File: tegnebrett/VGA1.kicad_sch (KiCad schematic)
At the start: 47 parts, among them J4 DA15_Socket

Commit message: feat: add 100MHz oscillator footprint
Additionally add the footprint to PCB.
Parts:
- J4: footprint (none) -> tegnebrett_modules:AMPHENOL_L77HDE15SD1CH4RHNVGA
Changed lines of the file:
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@@
 			)
 		)
-		(property "Footprint" ""
+		(property "Footprint" "tegnebrett_modules:AMPHENOL_L77HDE15SD1CH4RHNVGA"
 			(at 255.27 118.11 0)
 			(effects

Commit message: feat: add VGA Transceiver footprint
Additionally add VGA Transceiver to PCB layout.
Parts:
- U6: value ~ -> VGA Transceiver; footprint (none) -> tegnebrett_modules:SOP65P640X120-20N
- U7: value ~ -> VGA Transciever; footprint (none) -> tegnebrett_modules:SOP65P640X120-20N
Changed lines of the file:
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@@
 			)
 		)
-		(property "Value" "~"
+		(property "Value" "VGA Transciever"
 			(at 85.9633 128.27 0)
 			(effects
@@
 			)
 		)
-		(property "Footprint" ""
+		(property "Footprint" "tegnebrett_modules:SOP65P640X120-20N"
 			(at 78.74 128.27 0)
 			(effects
@@
 			)
 		)
-		(property "Value" "~"
+		(property "Value" "VGA Transceiver"
 			(at 80.8833 38.1 0)
 			(effects
@@
 			)
 		)
-		(property "Footprint" ""
+		(property "Footprint" "tegnebrett_modules:SOP65P640X120-20N"
 			(at 73.66 38.1 0)
 			(effects

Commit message: feat: add footprint for each capacitor
It's all 0805, 1206 or 1210 hand soldering variants.
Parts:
- C87, C88, C89, C90: footprint (none) -> Capacitor_SMD:C_0805_2012Metric_Pad1.18x1.45mm_HandSolder
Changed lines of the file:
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@@
 			)
 		)
-		(property "Footprint" ""
+		(property "Footprint" "Capacitor_SMD:C_0805_2012Metric_Pad1.18x1.45mm_HandSolder"
 			(at 86.0552 119.38 0)
 			(effects
@@
 			)
 		)
-		(property "Footprint" ""
+		(property "Footprint" "Capacitor_SMD:C_0805_2012Metric_Pad1.18x1.45mm_HandSolder"
 			(at 80.9752 29.21 0)
 			(effects
@@
 			)
 		)
-		(property "Footprint" ""
+		(property "Footprint" "Capacitor_SMD:C_0805_2012Metric_Pad1.18x1.45mm_HandSolder"
 			(at 69.5452 29.21 0)
 			(effects
@@
 			)
 		)
-		(property "Footprint" ""
+		(property "Footprint" "Capacitor_SMD:C_0805_2012Metric_Pad1.18x1.45mm_HandSolder"
 			(at 74.6252 119.38 0)
 			(effects

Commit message: feat: add footprint to resistors
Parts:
- R23, R24, R25, R26, R27, R28, R29, R30, R31, R32, R33, R34, R35, R36, R37, R38, R39, R40, R41, R42, R43, R44, R45, R46, R47, R48, R49, R50, R51, R52, R53, R54, R55, R56, R57, R58, R59, R60, R61, R62: footprint (none) -> Resistor_SMD:R_0805_2012Metric_Pad1.20x1.40mm_HandSolder
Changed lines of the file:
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@@
 			)
 		)
-		(property "Footprint" ""
+		(property "Footprint" "Resistor_SMD:R_0805_2012Metric_Pad1.20x1.40mm_HandSolder"
 			(at 35.052 171.45 90)
 			(effects
@@
 			)
 		)
-		(property "Footprint" ""
+		(property "Footprint" "Resistor_SMD:R_0805_2012Metric_Pad1.20x1.40mm_HandSolder"
 			(at 38.862 81.28 90)
 			(effects
@@
 			)
 		)
-		(property "Footprint" ""
+		(property "Footprint" "Resistor_SMD:R_0805_2012Metric_Pad1.20x1.40mm_HandSolder"
 			(at 125.222 54.61 90)
 			(effects
@@
 			)
 		)
-		(property "Footprint" ""
+		(property "Footprint" "Resistor_SMD:R_0805_2012Metric_Pad1.20x1.40mm_HandSolder"
 			(at 125.222 31.75 90)
 			(effects
@@
 			)
 		)
-		(property "Footprint" ""
+		(property "Footprint" "Resistor_SMD:R_0805_2012Metric_Pad1.20x1.40mm_HandSolder"
 			(at 166.37 62.738 90)
 			(effects
@@
 			)
 		)
-		(property "Footprint" ""
+		(property "Footprint" "Resistor_SMD:R_0805_2012Metric_Pad1.20x1.40mm_HandSolder"
 			(at 115.57 103.378 90)
 			(effects
@@
 			)
 		)
-		(property "Footprint" ""
+		(property "Footprint" "Resistor_SMD:R_0805_2012Metric_Pad1.20x1.40mm_HandSolder"
 			(at 49.022 35.56 90)
 			(effects
@@
 			)
 		)
-		(property "Footprint" ""
+		(property "Footprint" "Resistor_SMD:R_0805_2012Metric_Pad1.20x1.40mm_HandSolder"
 			(at 115.57 39.878 90)
 			(effects
@@
 			)
 		)
-		(property "Footprint" ""
+		(property "Footprint" "Resistor_SMD:R_0805_2012Metric_Pad1.20x1.40mm_HandSolder"
 			(at 31.242 35.56 90)
 			(effects
@@
 			)
 		)
-		(property "Footprint" ""
+		(property "Footprint" "Resistor_SMD:R_0805_2012Metric_Pad1.20x1.40mm_HandSolder"
 			(at 40.132 35.56 90)
 			(effects
@@
 			)
 		)
-		(property "Footprint" ""
+		(property "Footprint" "Resistor_SMD:R_0805_2012Metric_Pad1.20x1.40mm_HandSolder"
 			(at 125.222 118.11 90)
 			(effects
@@
 			)
 		)
-		(property "Footprint" ""
+		(property "Footprint" "Resistor_SMD:R_0805_2012Metric_Pad1.20x1.40mm_HandSolder"
 			(at 115.57 51.308 90)
 			(effects
@@
 			)
 		)
-		(property "Footprint" ""
+		(property "Footprint" "Resistor_SMD:R_0805_2012Metric_Pad1.20x1.40mm_HandSolder"
 			(at 237.49 124.968 90)
 			(effects
@@
 			)
 		)
-		(property "Footprint" ""
+		(property "Footprint" "Resistor_SMD:R_0805_2012Metric_Pad1.20x1.40mm_HandSolder"
 			(at 43.942 171.45 90)
 			(effects
@@
 			)
 		)
-		(property "Footprint" ""
+		(property "Footprint" "Resistor_SMD:R_0805_2012Metric_Pad1.20x1.40mm_HandSolder"
 			(at 125.222 129.54 90)
 			(effects
@@
 			)
 		)
-		(property "Footprint" ""
+		(property "Footprint" "Resistor_SMD:R_0805_2012Metric_Pad1.20x1.40mm_HandSolder"
 			(at 176.022 54.61 90)
 			(effects
@@
 			)
 		)
-		(property "Footprint" ""
+		(property "Footprint" "Resistor_SMD:R_0805_2012Metric_Pad1.20x1.40mm_HandSolder"
 			(at 115.57 62.738 90)
 			(effects
@@
 			)
 		)
-		(property "Footprint" ""
+		(property "Footprint" "Resistor_SMD:R_0805_2012Metric_Pad1.20x1.40mm_HandSolder"
 			(at 54.102 125.73 90)
 			(effects
@@
 			)
 		)
-		(property "Footprint" ""
+		(property "Footprint" "Resistor_SMD:R_0805_2012Metric_Pad1.20x1.40mm_HandSolder"
 			(at 115.57 114.808 90)
 			(effects
@@
 			)
 		)
-		(property "Footprint" ""
+		(property "Footprint" "Resistor_SMD:R_0805_2012Metric_Pad1.20x1.40mm_HandSolder"
 			(at 176.022 43.18 90)
 			(effects
@@
 			)
 		)
-		(property "Footprint" ""
+		(property "Footprint" "Resistor_SMD:R_0805_2012Metric_Pad1.20x1.40mm_HandSolder"
 			(at 125.222 106.68 90)
 			(effects
@@
 			)
 		)
-		(property "Footprint" ""
+		(property "Footprint" "Resistor_SMD:R_0805_2012Metric_Pad1.20x1.40mm_HandSolder"
 			(at 166.37 74.168 90)
 			(effects
@@
 			)
 		)
-		(property "Footprint" ""
+		(property "Footprint" "Resistor_SMD:R_0805_2012Metric_Pad1.20x1.40mm_HandSolder"
 			(at 166.37 41.148 90)
 			(effects
@@
 			)
 		)
-		(property "Footprint" ""
+		(property "Footprint" "Resistor_SMD:R_0805_2012Metric_Pad1.20x1.40mm_HandSolder"
 			(at 125.222 66.04 90)
 			(effects
@@
 			)
 		)
-		(property "Footprint" ""
+		(property "Footprint" "Resistor_SMD:R_0805_2012Metric_Pad1.20x1.40mm_HandSolder"
 			(at 47.752 81.28 90)
 			(effects
@@
 			)
 		)
-		(property "Footprint" ""
+		(property "Footprint" "Resistor_SMD:R_0805_2012Metric_Pad1.20x1.40mm_HandSolder"
 			(at 45.212 125.73 90)
 			(effects
@@
 			)
 		)
-		(property "Footprint" ""
+		(property "Footprint" "Resistor_SMD:R_0805_2012Metric_Pad1.20x1.40mm_HandSolder"
 			(at 29.972 81.28 90)
 			(effects
@@
 			)
 		)
-		(property "Footprint" ""
+		(property "Footprint" "Resistor_SMD:R_0805_2012Metric_Pad1.20x1.40mm_HandSolder"
 			(at 57.912 35.56 90)
 			(effects
@@
 			)
 		)
-		(property "Footprint" ""
+		(property "Footprint" "Resistor_SMD:R_0805_2012Metric_Pad1.20x1.40mm_HandSolder"
 			(at 166.37 51.308 90)
 			(effects
@@
 			)
 		)
-		(property "Footprint" ""
+		(property "Footprint" "Resistor_SMD:R_0805_2012Metric_Pad1.20x1.40mm_HandSolder"
 			(at 176.022 77.47 90)
 			(effects
@@
 			)
 		)
-		(property "Footprint" ""
+		(property "Footprint" "Resistor_SMD:R_0805_2012Metric_Pad1.20x1.40mm_HandSolder"
 			(at 115.57 93.218 90)
 			(effects
@@
 			)
 		)
-		(property "Footprint" ""
+		(property "Footprint" "Resistor_SMD:R_0805_2012Metric_Pad1.20x1.40mm_HandSolder"
 			(at 56.642 81.28 90)
 			(effects
@@
 			)
 		)
-		(property "Footprint" ""
+		(property "Footprint" "Resistor_SMD:R_0805_2012Metric_Pad1.20x1.40mm_HandSolder"
 			(at 115.57 126.238 90)
 			(effects
@@
 			)
 		)
-		(property "Footprint" ""
+		(property "Footprint" "Resistor_SMD:R_0805_2012Metric_Pad1.20x1.40mm_HandSolder"
 			(at 176.022 66.04 90)
 			(effects
@@
 			)
 		)
-		(property "Footprint" ""
+		(property "Footprint" "Resistor_SMD:R_0805_2012Metric_Pad1.20x1.40mm_HandSolder"
 			(at 62.992 125.73 90)
 			(effects
@@
 			)
 		)
-		(property "Footprint" ""
+		(property "Footprint" "Resistor_SMD:R_0805_2012Metric_Pad1.20x1.40mm_HandSolder"
 			(at 115.57 29.718 90)
 			(effects
@@
 			)
 		)
-		(property "Footprint" ""
+		(property "Footprint" "Resistor_SMD:R_0805_2012Metric_Pad1.20x1.40mm_HandSolder"
 			(at 125.222 43.18 90)
 			(effects
@@
 			)
 		)
-		(property "Footprint" ""
+		(property "Footprint" "Resistor_SMD:R_0805_2012Metric_Pad1.20x1.40mm_HandSolder"
 			(at 36.322 125.73 90)
 			(effects
@@
 			)
 		)
-		(property "Footprint" ""
+		(property "Footprint" "Resistor_SMD:R_0805_2012Metric_Pad1.20x1.40mm_HandSolder"
 			(at 237.49 130.048 90)
 			(effects
@@
 			)
 		)
-		(property "Footprint" ""
+		(property "Footprint" "Resistor_SMD:R_0805_2012Metric_Pad1.20x1.40mm_HandSolder"
 			(at 125.222 95.25 90)
 			(effects

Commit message: refactor: re-annotate schematic labels
References for schematic capacitors (for example C74 -> C2), etc.
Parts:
- renumbered C87 to C23, C88 to C24, C89 to C25, C90 to C26, J4 to J8, R23 to R28, R24 to R29, R25 to R30, R26 to R31, R27 to R32, R28 to R33, R29 to R34, R30 to R35, R31 to R36, R32 to R37, R33 to R38, R34 to R39, R35 to R40, R36 to R41, R37 to R42, R38 to R43, R39 to R44, R40 to R45, R41 to R46, R42 to R47, R43 to R48, R44 to R49, R45 to R50, R46 to R51, R47 to R52, R48 to R53, R49 to R54, R50 to R55, R51 to R56, R52 to R57, R53 to R58, R54 to R59, R55 to R60, R56 to R61, R57 to R62, R58 to R63, R59 to R64, R60 to R65, R61 to R66, R62 to R67, U6 to U5, U7 to U6

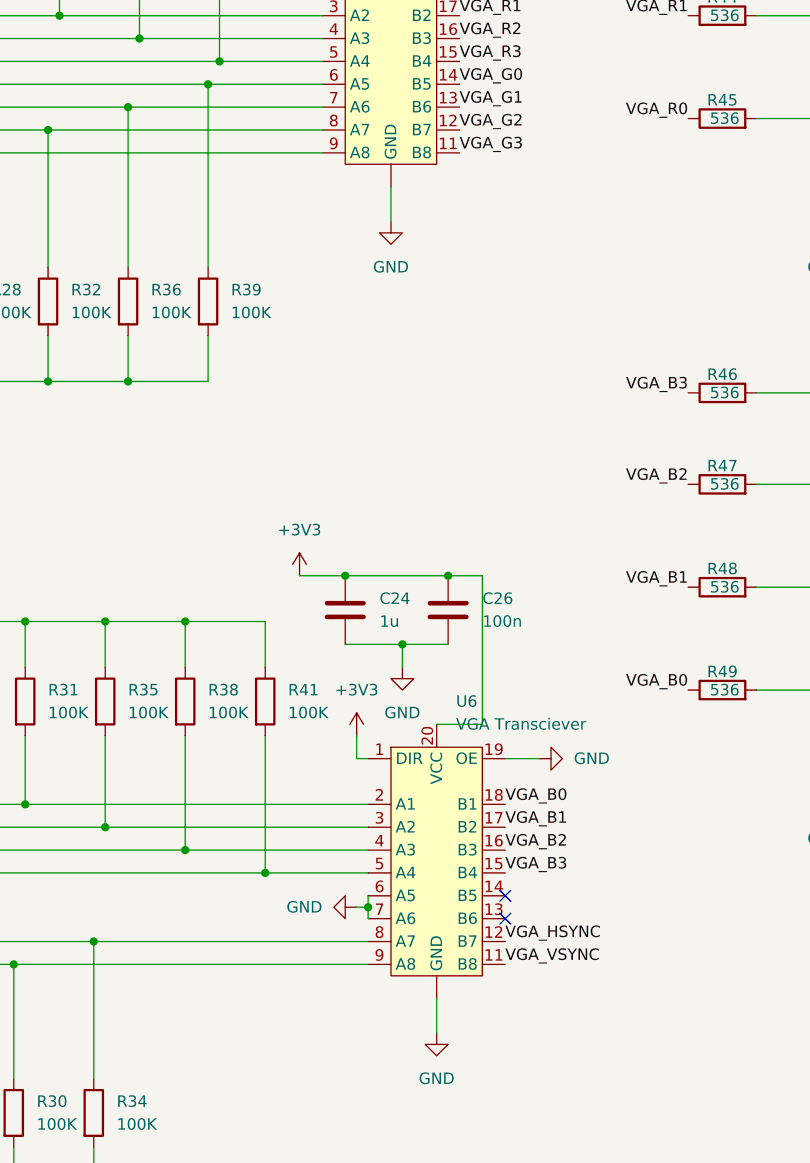
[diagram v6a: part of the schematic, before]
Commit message: feat: update VGA transceiver symbol
The bottom ground pin didn't have a number attached to it.
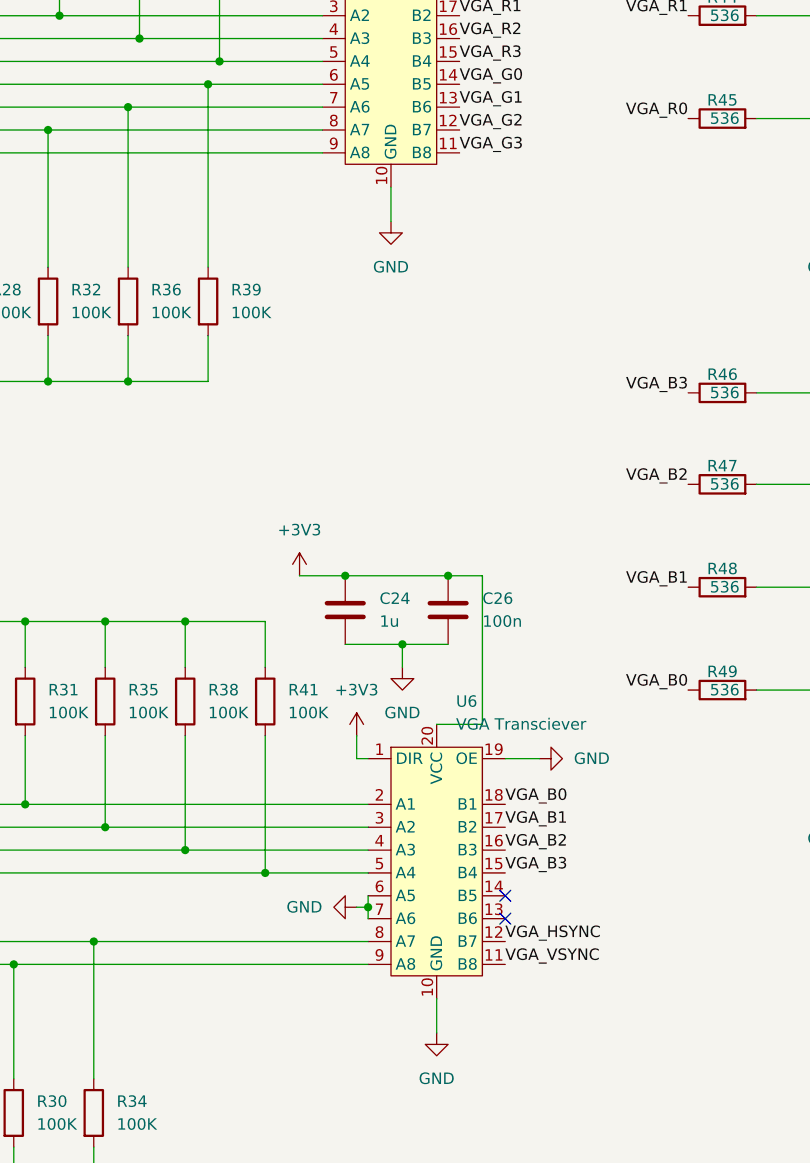
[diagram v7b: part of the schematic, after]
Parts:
- U5, U6: symbol XC7A100T-2FTG256I:SN74ALVC245PWR -> tegnebrett_symbols:SN74ALVC245PWR
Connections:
- net GND: now also U5.10 (GND), U6.10 (GND); no longer U5. (GND), U6. (GND)
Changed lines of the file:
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@@
 	)
 	(symbol
-		(lib_id "XC7A100T-2FTG256I:SN74ALVC245PWR")
+		(lib_id "tegnebrett_symbols:SN74ALVC245PWR")
 		(at 78.74 128.27 0)
 		(unit 1)
@@
 		(pin "20"
 		)
-		(pin ""
+		(pin "10"
 		)
 		(instances
@@
 	)
 	(symbol
-		(lib_id "XC7A100T-2FTG256I:SN74ALVC245PWR")
+		(lib_id "tegnebrett_symbols:SN74ALVC245PWR")
 		(at 73.66 38.1 0)
 		(unit 1)
@@
 		(pin "20"
 		)
-		(pin ""
-		)
-		(instances
+		(pin "10"
+		)
+		(instances
